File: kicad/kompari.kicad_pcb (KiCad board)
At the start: 2 copper layers, 28.4 x 100 mm, 34 parts, among them J1 Thonkiconn_Mono_Jack, J2 Thonkiconn_Mono_Jack, J3 Conn_02x05_Odd_Even, J4 Thonkiconn_Mono_Jack, P1 100K, P2 100K, P3 100K, SW1 SW_SPDT, U1 TL074

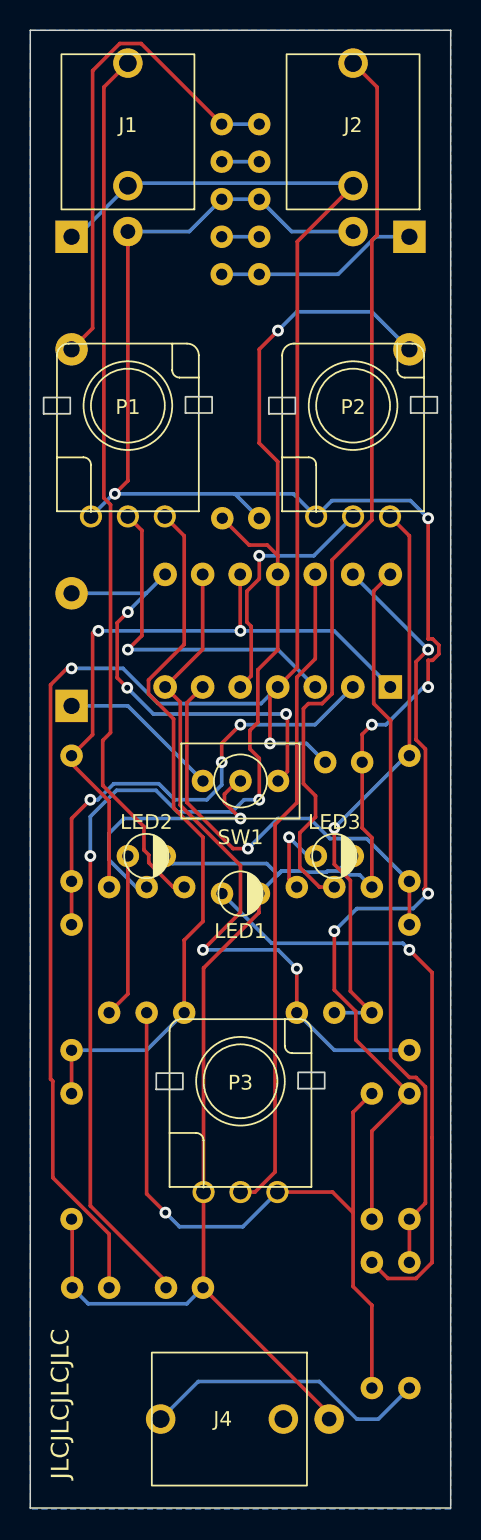
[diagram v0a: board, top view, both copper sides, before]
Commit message: Optimise PCB trace spacing, fix switch
The switch was previously the wrong way round, so left would be bipolar when it should be left for unipolar. This has been fixed as well as general increasing of spacing between traces
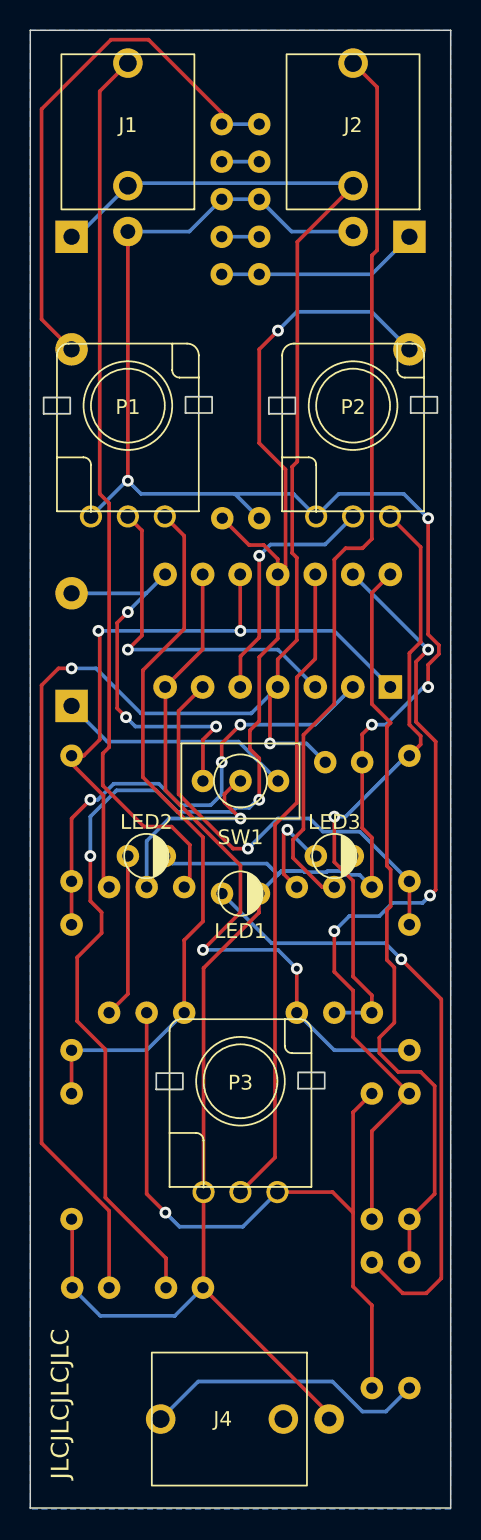
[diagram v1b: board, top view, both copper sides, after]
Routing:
- net Net-(D3-Pad2): track 11.0 -> 16.1 mm
- net Net-(R15-Pad1): track 18.0 -> 13.6 mm
- net Net-(D3-Pad1): track 30.7 -> 26.7 mm
- net -12V: track 96.2 -> 99.2 mm
- net Net-(D1-Pad1): track 33.7 -> 36.6 mm
- net Net-(R6-Pad2): track 49.2 -> 51.7 mm
- net Net-(P2-Pad3): track 39.9 -> 41.6 mm
- net +12V: track 124.7 -> 126.3 mm
- net Net-(LED1-Pad1): track 41.0 -> 42.7 mm
- net Net-(J1-Pad3): track 59.6 -> 60.7 mm
- net Net-(LED3-Pad1): track 5.92 -> 7.01 mm
- net Net-(R1-Pad2): track 32.4 -> 33.1 mm
- net Net-(P3-Pad2): track 44.5 -> 43.9 mm

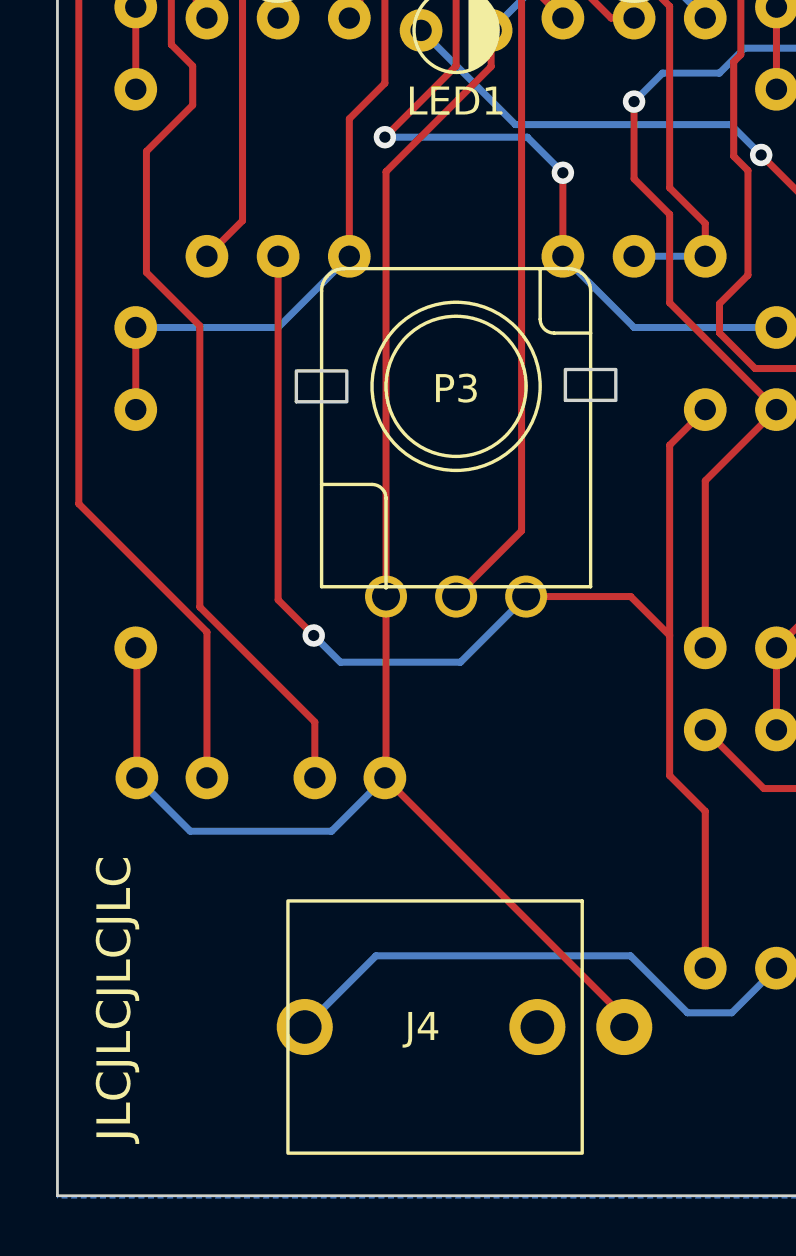
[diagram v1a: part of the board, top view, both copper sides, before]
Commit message: Add version number to PCB
Add version number 1.0 to PCB
Rotate C1 and C2 to not cover up website silkscreen
Export Gerbers
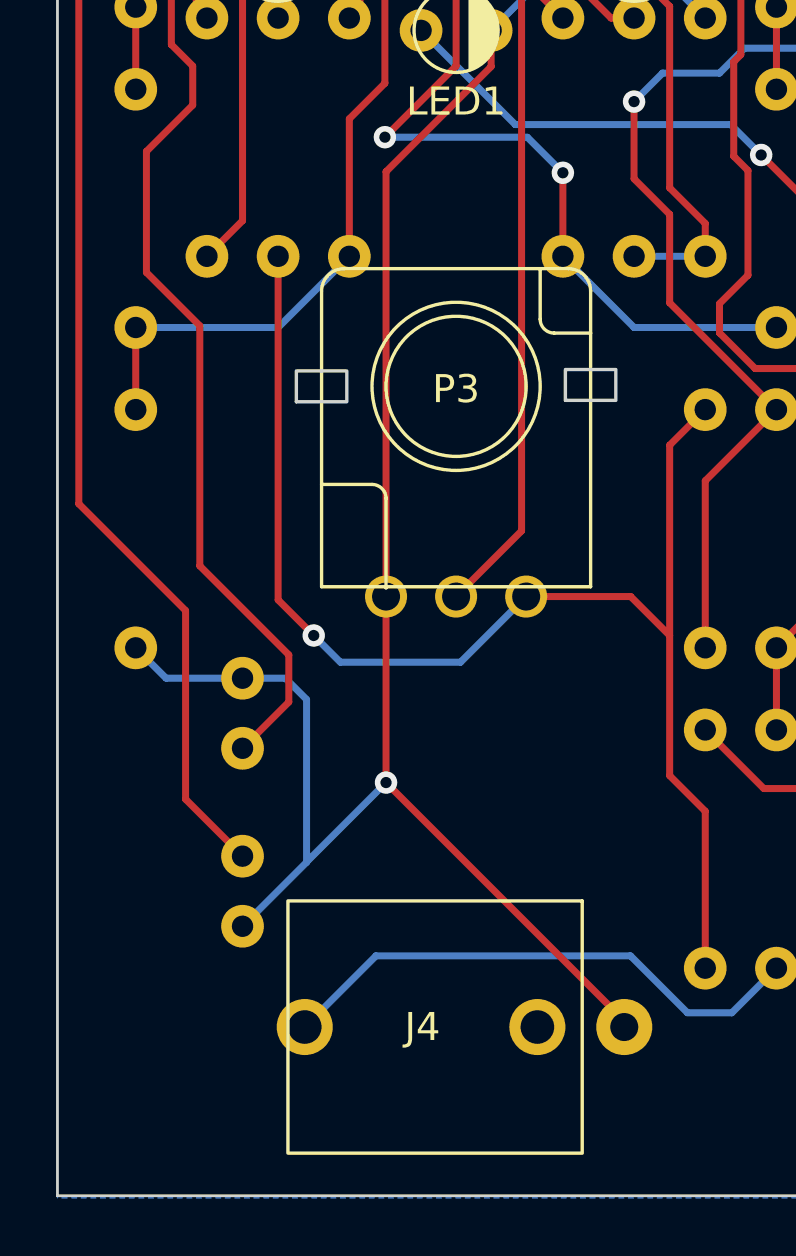
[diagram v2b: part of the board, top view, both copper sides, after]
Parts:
- moved C2 6.20 mm to (7.62, 81.5), turned to -90 degrees
- moved C1 3.07 mm to (7.62, 87.9), turned to -90 degrees
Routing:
- net Earth: track 166.0 -> 170.8 mm, vias 4 -> 5
- net +12V: track 126.3 -> 129.7 mm
- net -12V: track 99.2 -> 98.4 mm
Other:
- board text added: "version 1.0"

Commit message: PCB improvements
trace spacing
wider traces for unprotected power lines
potentiometer lug holes widened
regenerate gerbers + bom
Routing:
- net Earth: track 170.8 -> 71.4 mm, vias 5 -> 1
- net +12V: track 129.7 -> 135.2 mm
- net -12V: track 98.4 -> 97.1 mm
- net Net-(R15-Pad1): track 13.6 -> 12.6 mm
- net Net-(R5-Pad2): track 55.0 -> 54.4 mm
- net Net-(P2-Pad2): track 16.9 -> 17.4 mm
